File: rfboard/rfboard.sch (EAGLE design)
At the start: 17 parts, among them U1 MAX1555

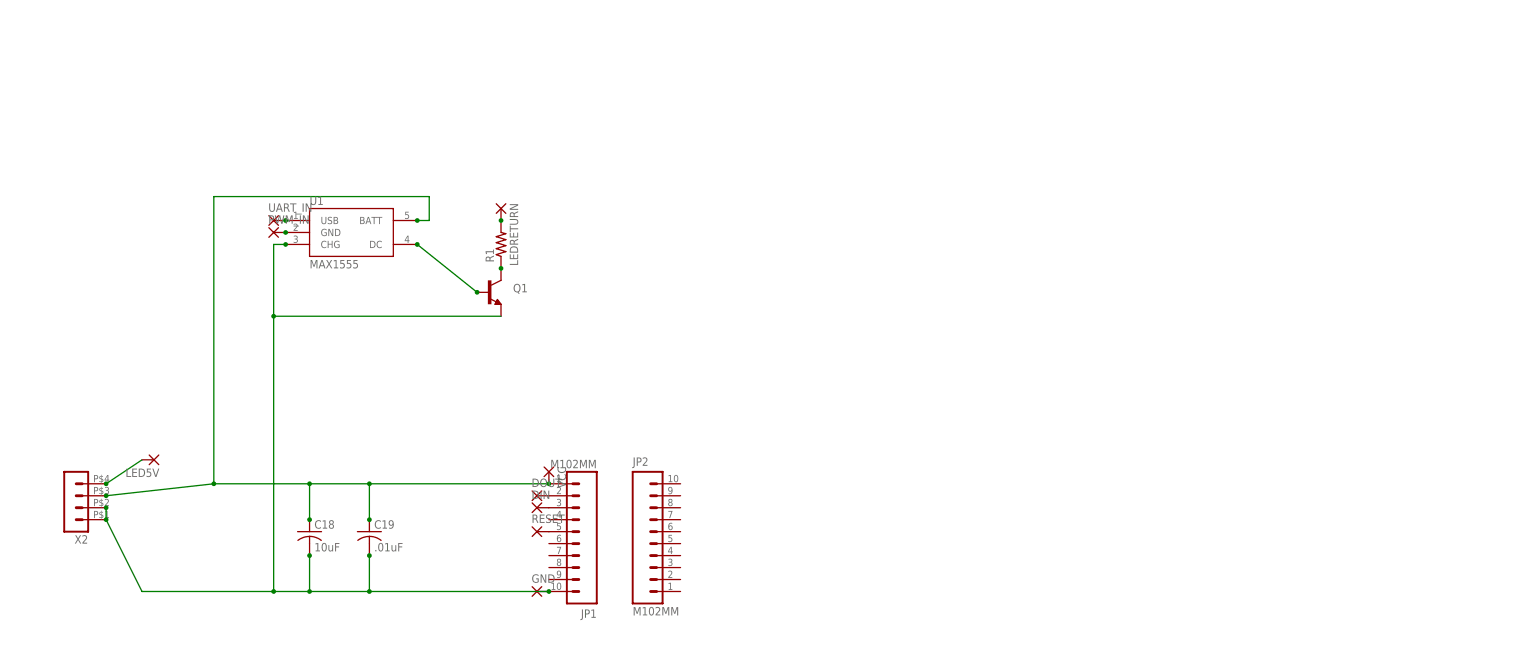
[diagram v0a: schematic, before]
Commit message: changing the RF board to include voltage dividers
- rearranged board to include pin headers
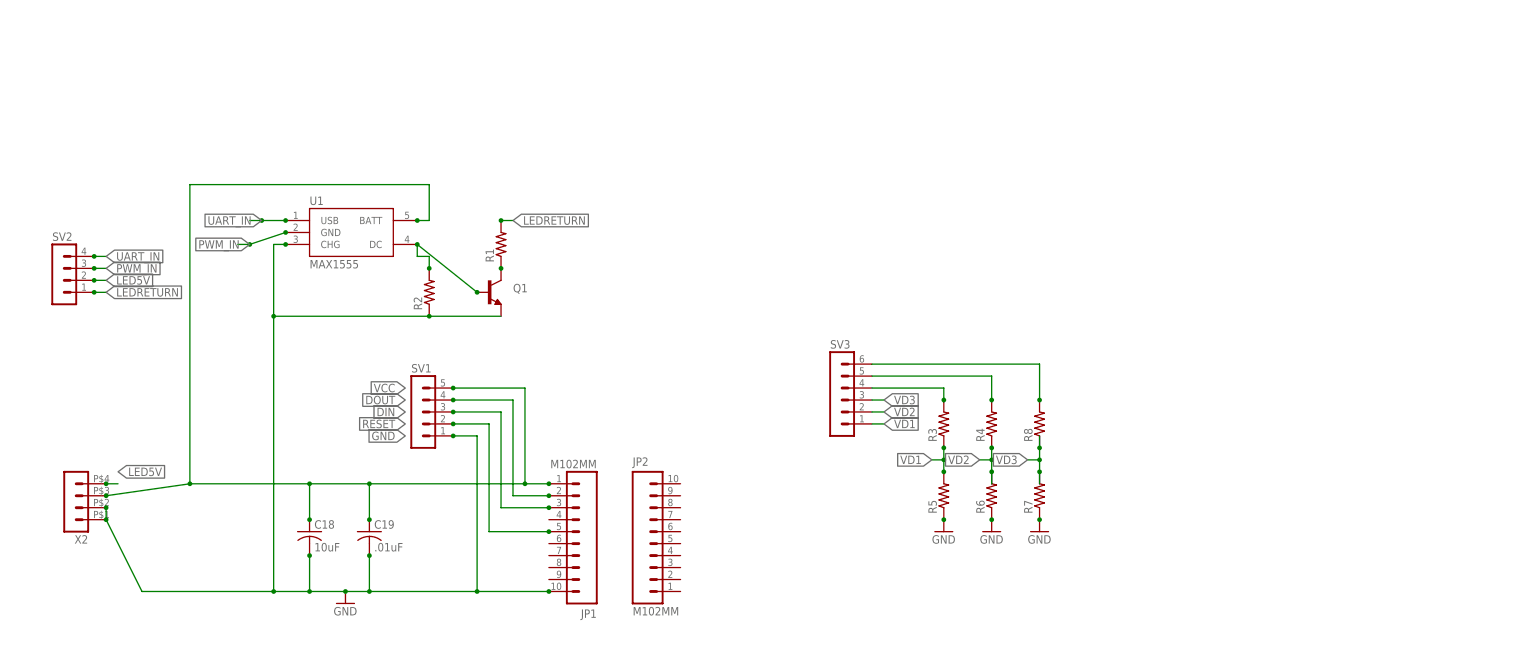
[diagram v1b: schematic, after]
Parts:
- removed DIN, DOUT, GND, LED5V, LEDRETURN, PWM_IN, RESET, UART_IN, VCC: (no value), wirepad:1,6/0,9
- added R2, R3, R4, R5, R6, R7, R8: (no value), rcl:R-US_R1206
- added SV1: (no value), con-lstb:MA05-1
- added SV2: (no value), con-lstb:MA04-1
- added SV3: (no value), con-lstb:MA06-1
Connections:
- removed net 3.3V-2: C18.1, C19.1, JP1.1, U1.BATT, VCC.P, X2.3
- removed net GND2: C18.2, C19.2, GND.P, JP1.10, Q1.E, U1.CHG, X2.1, X2.2
- removed net N$1: DOUT.P, JP1.2
- removed net N$2: DIN.P, JP1.3
- removed net N$4: JP1.5, RESET.P
- removed net N$6: U1.USB, UART_IN.P
- removed net N$7: PWM_IN.P, U1.GND
- removed net N$8: LEDRETURN.P, R1.2
- removed net N$9: LED5V.P, X2.4
- new net DIN: JP1.3, SV1.3
- new net DOUT: JP1.2, SV1.4
- new net GND: C18.2, C19.2, JP1.10, Q1.E, R2.1, R5.1, R6.1, R7.1, SV1.1, U1.CHG, X2.1, X2.2
- new net LED5V: SV2.2, X2.4
- new net LEDRETURN: R1.2, SV2.1
- new net PWM_IN: SV2.3, U1.GND
- new net RESET: JP1.5, SV1.2
- new net UART_IN: SV2.4, U1.USB
- new net VCC: C18.1, C19.1, JP1.1, SV1.5, U1.BATT, X2.3
- new net VD1: R3.1, R5.2, SV3.1
- new net VD2: R4.1, R6.2, SV3.2
- new net VD3: R7.2, R8.1, SV3.3
- new net V_1: R3.2, SV3.4
- new net V_2: R4.2, SV3.5
- new net V_3: R8.2, SV3.6
- net N$3: now also R2.2

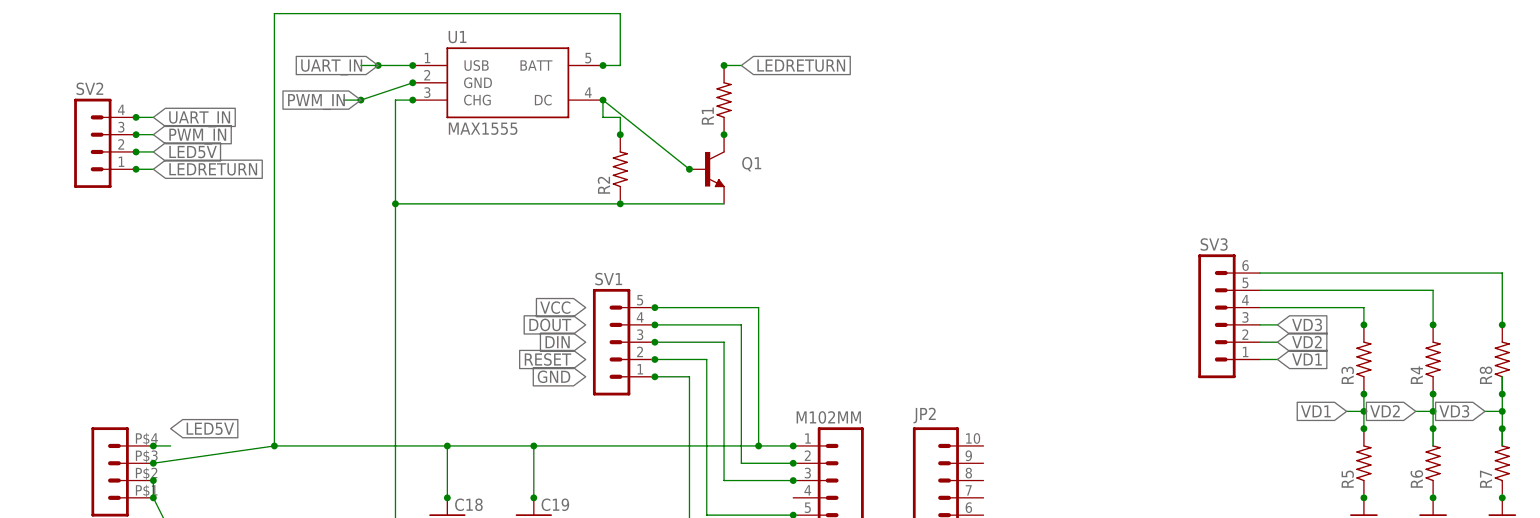
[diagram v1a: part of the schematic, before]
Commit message: changed headers and finished board
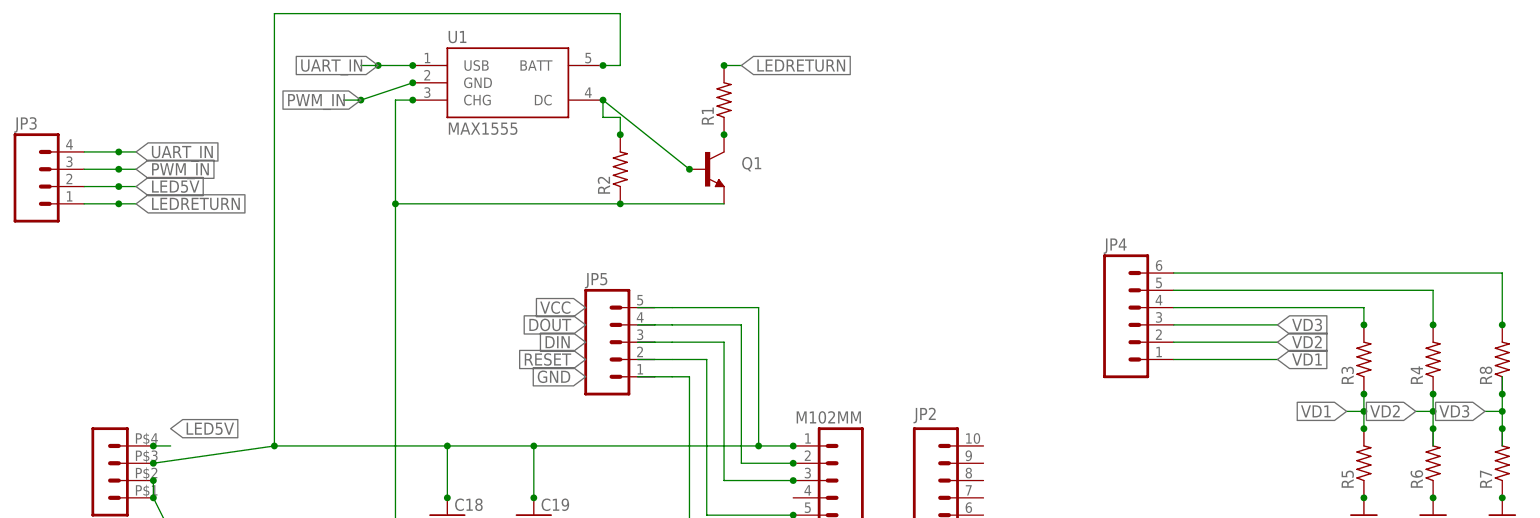
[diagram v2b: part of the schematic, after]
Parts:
- removed SV1: (no value), con-lstb:MA05-1
- removed SV2: (no value), con-lstb:MA04-1
- removed SV3: (no value), con-lstb:MA06-1
- added JP3: (no value), SparkFun-Connectors:M04LOCK
- added JP4: (no value), SparkFun-Connectors:M06LOCK
- added JP5: (no value), SparkFun-Connectors:M05LOCK
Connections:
- net DIN: now also JP5.3; no longer SV1.3
- net DOUT: now also JP5.4; no longer SV1.4
- net GND: now also JP5.1; no longer SV1.1
- net LED5V: now also JP3.2; no longer SV2.2
- net LEDRETURN: now also JP3.1; no longer SV2.1
- net PWM_IN: now also JP3.3; no longer SV2.3
- net RESET: now also JP5.2; no longer SV1.2
- net UART_IN: now also JP3.4; no longer SV2.4
- net VCC: now also JP5.5; no longer SV1.5
- net VD1: now also JP4.1; no longer SV3.1
- net VD2: now also JP4.2; no longer SV3.2
- net VD3: now also JP4.3; no longer SV3.3
- net V_1: now also JP4.4; no longer SV3.4
- net V_2: now also JP4.5; no longer SV3.5
- net V_3: now also JP4.6; no longer SV3.6

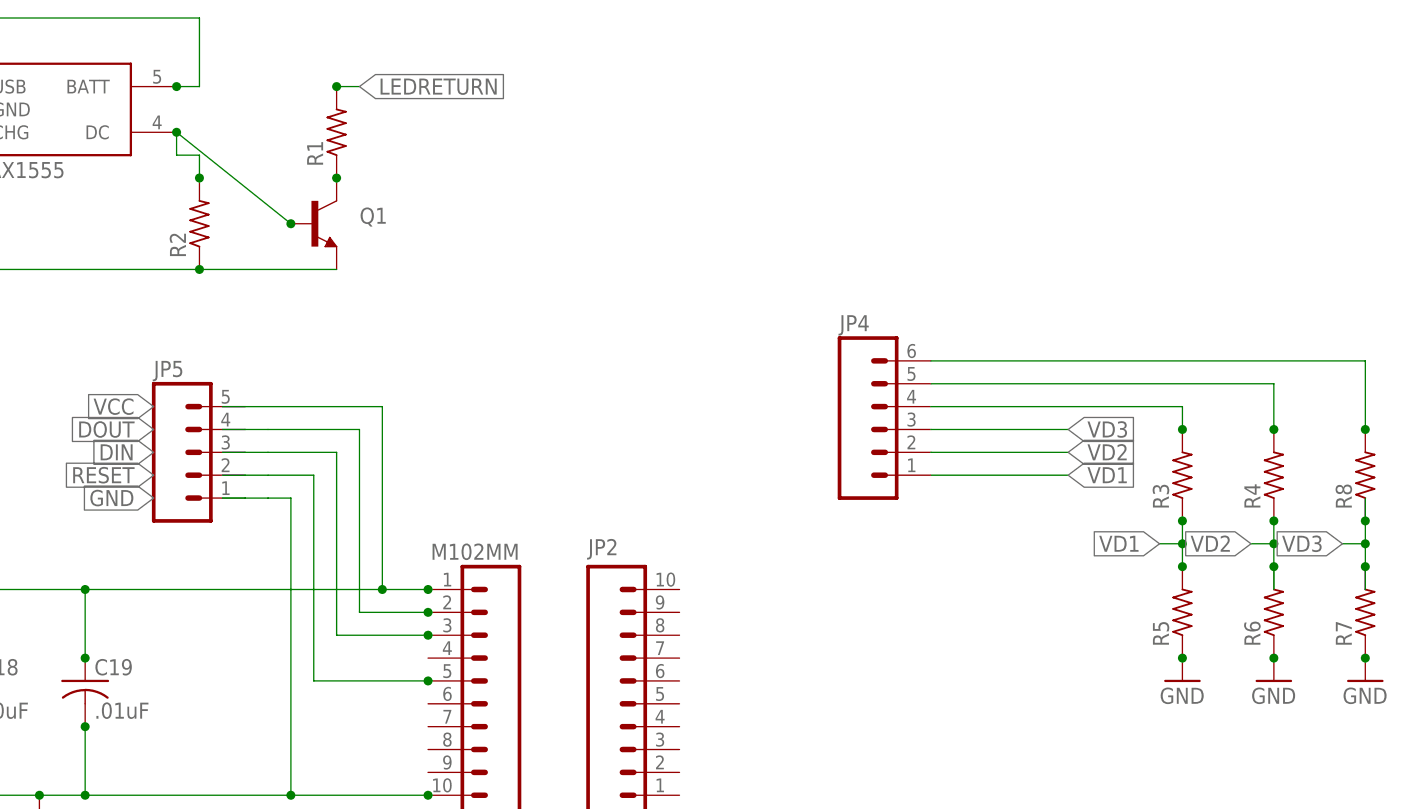
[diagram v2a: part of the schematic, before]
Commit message: Changes to layout and silk screen, new gerber files
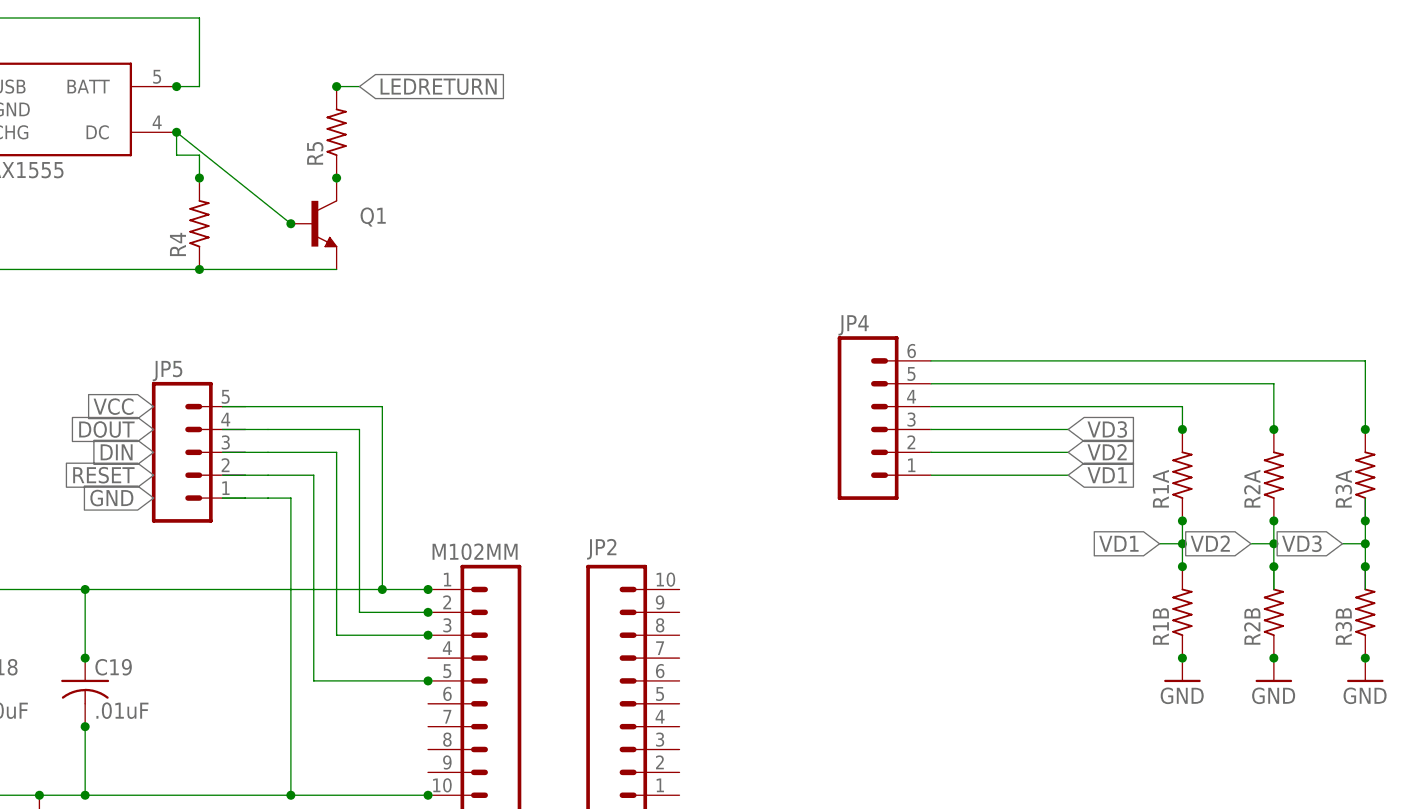
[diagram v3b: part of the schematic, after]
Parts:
- removed R1, R2: (no value), rcl:R-US_R1206
- added R1B, R2A: (no value), rcl:R-US_R1206
- renumbered R3 to R1A, R6 to R2B, R7 to R3B, R8 to R3A
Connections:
- net GND: now also R1B.1, R4.1; no longer R2.1, R5.1
- net LEDRETURN: now also R5.2; no longer R1.2
- net N$3: now also R4.2; no longer R2.2
- net N$5: now also R5.1; no longer R1.1
- net VD1: now also R1B.2; no longer R5.2
- net VD2: now also R2A.1; no longer R4.1
- net V_2: now also R2A.2; no longer R4.2
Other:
- moved on the sheet: R4, R5

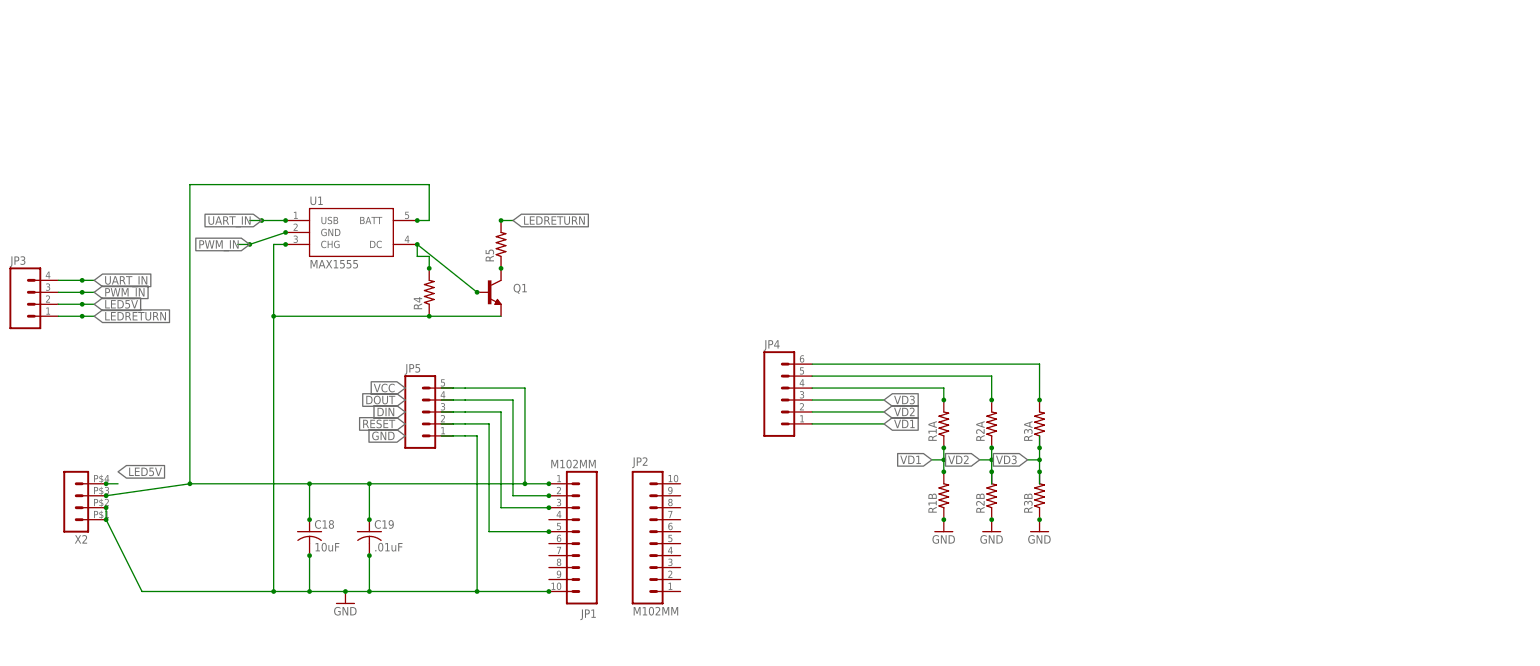
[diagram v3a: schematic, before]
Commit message: added ambient light sensor and 3 voltage dividers, new XBEE connection
-added the MONOLITHIC PHOTODIODE AND SINGLE-SUPPLY TRANSIMPEDANCE AMPLIFIER, ie OPT101 abmient light sensors
-added circuitry for the OPT101
-added header pin, labeled AMB_OUT, for the output of the OPT101
-added three extra voltage dividers for future DMS sensors
-added six 2mm 2pin headers for the DMS Sensors cables
--NOTE: the DMS sensor headers are currently GND, VCC, DATA from left to right
-changed XBEE connection to one 2mm 10pin header for new adaptor board
-change circuitry for proper connections
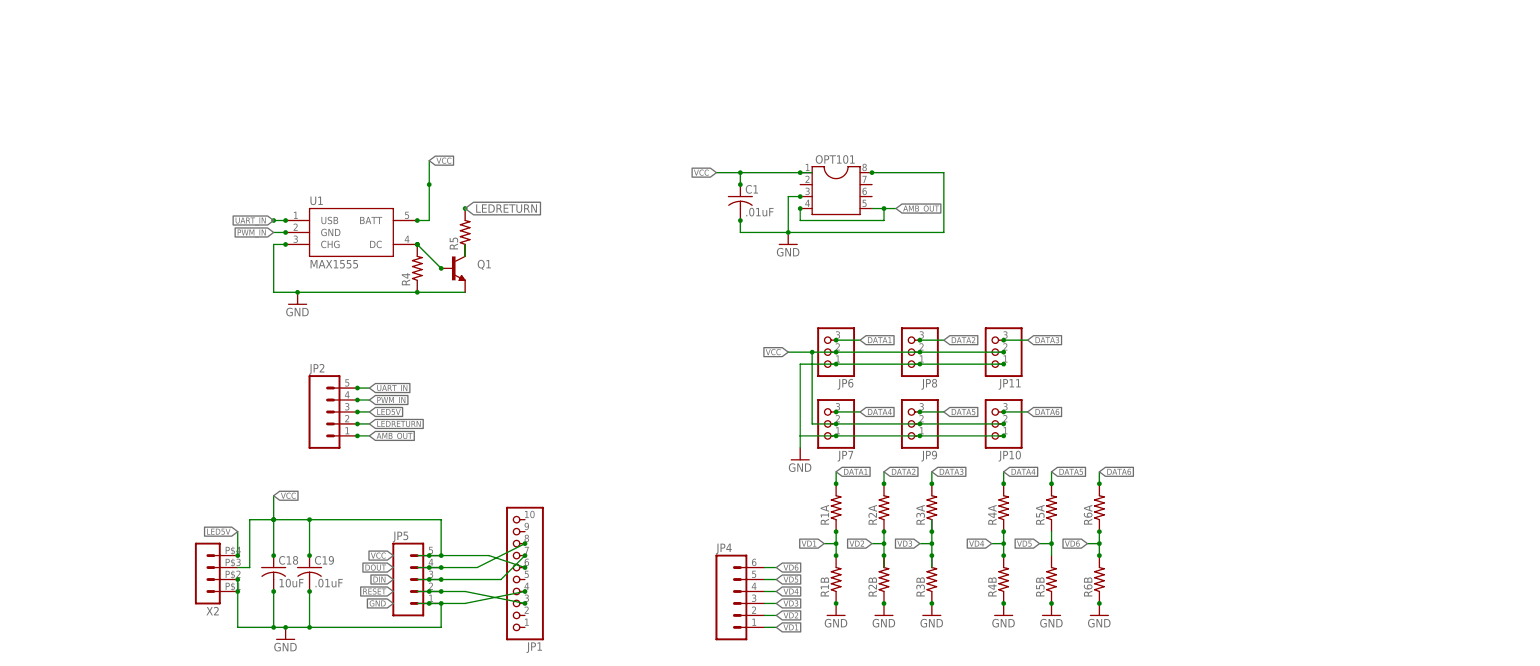
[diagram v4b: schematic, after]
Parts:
- removed JP3: (no value), SparkFun-Connectors:M04LOCK
- added C1: .01uF, rcl:C-USC0805K
- added JP10, JP11, JP6, JP7, JP8, JP9: (no value), pinhead-2:PINHD-1X03_2.00
- added OPT101: (no value), ic-package:DIL8
- added R4A, R4B, R5A, R5B, R6A, R6B: (no value), rcl:R-US_R1206
- JP1: value M102MM -> (none); device SparkFun-Connectors 2:M102MM -> pinhead-2:PINHD-1X10_2.00
- JP2: value M102MM -> (none); device SparkFun-Connectors 2:M102MM -> SparkFun-Connectors:M05LOCK
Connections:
- removed net V_1: JP4.4, R1A.2
- removed net V_2: JP4.5, R2A.2
- removed net V_3: JP4.6, R3A.2
- new net AMB_OUT: JP2.1, OPT101.4, OPT101.5
- new net DATA1: JP6.3, R1A.2
- new net DATA2: JP8.3, R2A.2
- new net DATA3: JP11.3, R3A.2
- new net DATA4: JP7.3, R4A.2
- new net DATA5: JP9.3, R5A.2
- new net DATA6: JP10.3, R6A.2
- new net VD4: JP4.4, R4A.1, R4B.2
- new net VD5: JP4.5, R5A.1, R5B.2
- new net VD6: JP4.6, R6A.1, R6B.2
- net DIN: now also JP1.7; no longer JP1.3
- net DOUT: now also JP1.8; no longer JP1.2
- net GND: now also C1.2, JP1.4, JP10.1, JP11.1, JP6.1, JP7.1, JP8.1, JP9.1, OPT101.3, OPT101.8, R4B.1, R5B.1, R6B.1; no longer JP1.10
- net LED5V: now also JP2.3; no longer JP3.2
- net LEDRETURN: now also JP2.2; no longer JP3.1
- net PWM_IN: now also JP2.4; no longer JP3.3
- net RESET: now also JP1.3; no longer JP1.5
- net UART_IN: now also JP2.5; no longer JP3.4
- net VCC: now also C1.1, JP1.6, JP10.2, JP11.2, JP6.2, JP7.2, JP8.2, JP9.2, OPT101.1; no longer JP1.1
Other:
- note added: "And Gate Circuit"
- note added: "Distance Sensors Voltage Division Circuit"
- note added: "This is the Ambient light sensor"
- note added: "XBee Circuit"
- moved on the sheet: C18, C19, JP4, JP5, Q1, R1A, R1B, R2A, R2B, R3A, R3B, R4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
